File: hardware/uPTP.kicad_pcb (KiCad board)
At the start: 2 copper layers, 40 x 50 mm, 56 parts, among them J1 UART_HDR, J2 PPS_UFL, J3 PPS_SMA, J4 HC-RJ45-055-7, J5 AUX_PWR, J6 PROG, U1 CH32V307WCU6, U2 TMI7301, U3 LMR16030SDDAR, U4 XC6206P332MR-G, U5 SI3404-A-GMR, X1 X50328MSB2GI

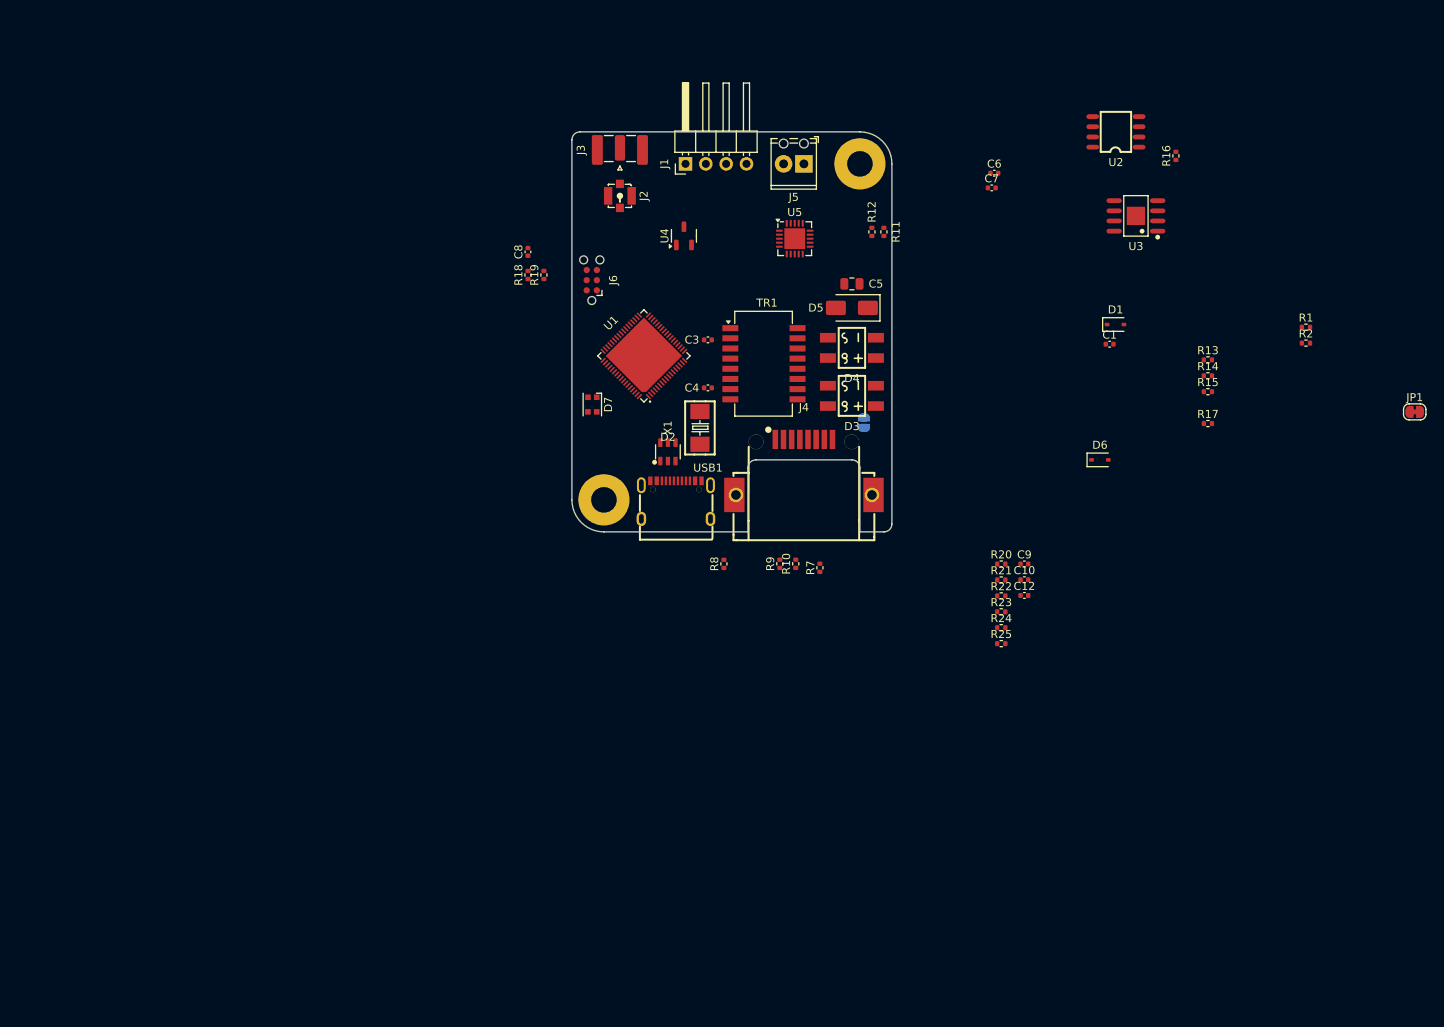
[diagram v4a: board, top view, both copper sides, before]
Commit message: Confirm all part footprints, start rought layout
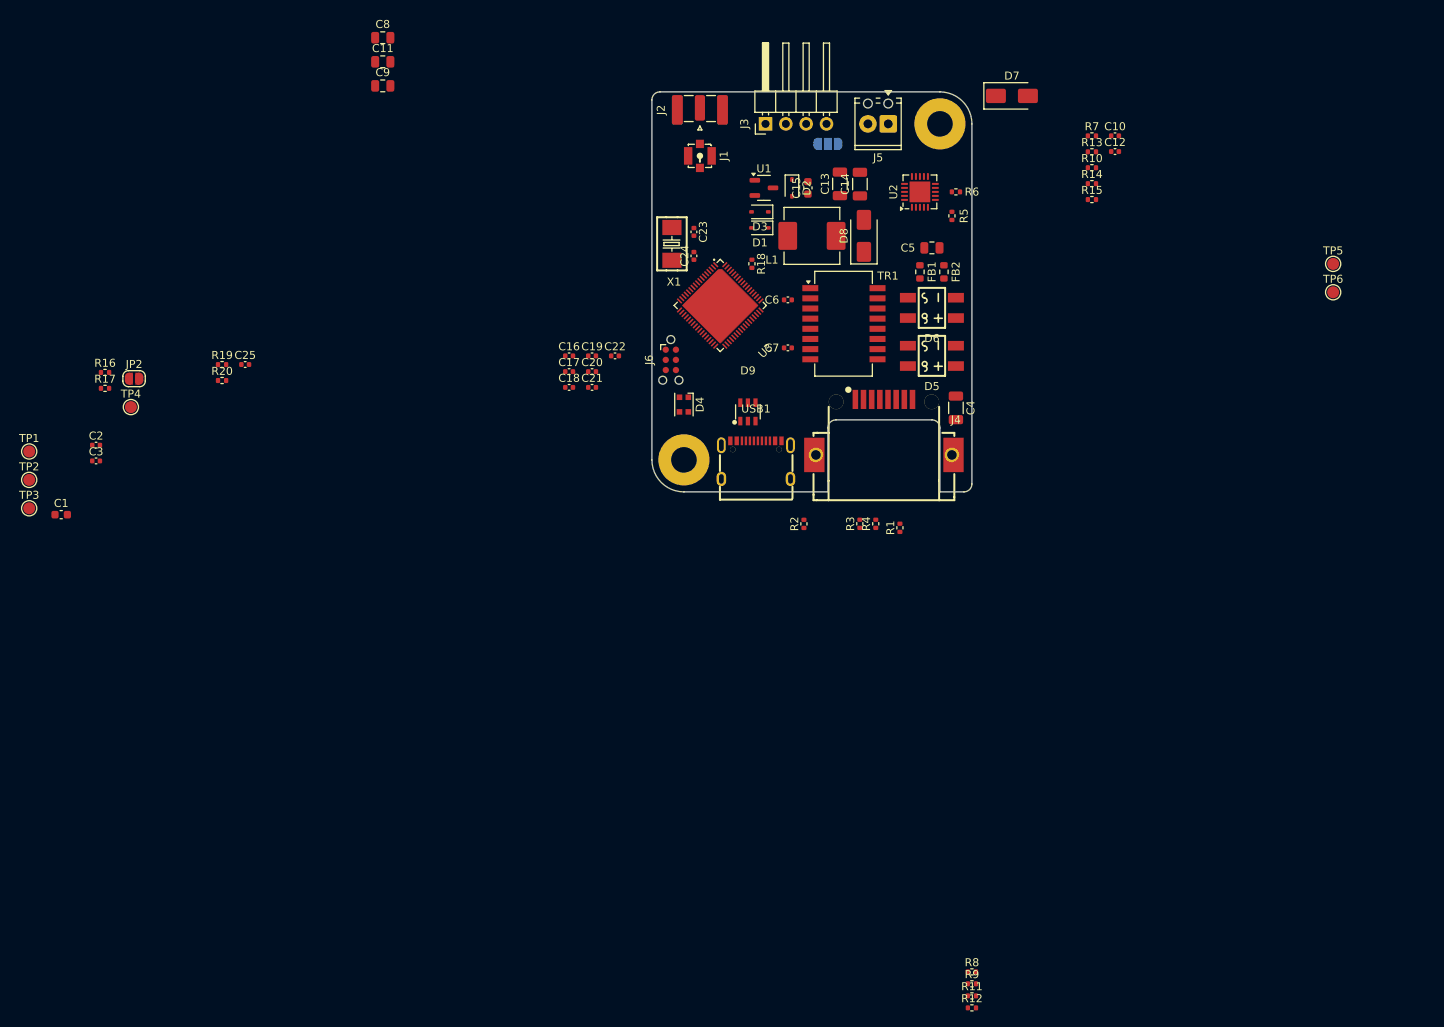
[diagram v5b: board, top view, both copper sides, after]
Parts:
- removed the C12 at (176.6, 137.9)
- removed the C6 at (172.8, 85.2)
- removed the C7 at (172.5, 87.0)
- removed the D5 at (155.0, 102.0)
- removed the D6 at (186.0, 121.0)
- removed the R1 at (211.8, 104.4)
- removed the R2 at (211.8, 106.4)
- removed R25: ?, Resistor_SMD:R_0402_1005Metric
- removed the U2 at (188.0, 80.0)
- removed U4: XC6206P332MR-G, Package_TO_SOT_SMD:SOT-23-3
- added C11: 10u, Capacitor_SMD:C_0805_2012Metric, F.Cu at (96.4, 71.2)
- added C13: 100u, Capacitor_SMD:C_1206_3216Metric, F.Cu at (153.5, 86.5)
- added C14: 100u, Capacitor_SMD:C_1206_3216Metric, F.Cu at (156.0, 86.5)
- added C15: 10u, Capacitor_SMD:C_0603_1608Metric, F.Cu at (149.5, 87.0)
- added C16: 100n, Capacitor_SMD:C_0402_1005Metric, F.Cu at (119.7, 108.0)
- added C17: 100n, Capacitor_SMD:C_0402_1005Metric, F.Cu at (119.7, 110.0)
- added C18: 100n, Capacitor_SMD:C_0402_1005Metric, F.Cu at (119.7, 111.9)
- added C19: 100n, Capacitor_SMD:C_0402_1005Metric, F.Cu at (122.5, 108.0)
- added C2: 100n, Capacitor_SMD:C_0402_1005Metric, F.Cu at (60.5, 119.2)
- added C20: 100n, Capacitor_SMD:C_0402_1005Metric, F.Cu at (122.5, 110.0)
- added C21: 100n, Capacitor_SMD:C_0402_1005Metric, F.Cu at (122.5, 111.9)
- added C22: 100n, Capacitor_SMD:C_0402_1005Metric, F.Cu at (125.4, 108.0)
- added C23: 20p, Capacitor_SMD:C_0402_1005Metric, F.Cu at (135.2, 92.5)
- added C24: 20p, Capacitor_SMD:C_0402_1005Metric, F.Cu at (135.2, 95.5)
- added C25: 100n, Capacitor_SMD:C_0402_1005Metric, F.Cu at (79.2, 109.1)
- added C3: 2.2u, Capacitor_SMD:C_0402_1005Metric, F.Cu at (60.5, 121.1)
- added C4: 1n, Capacitor_SMD:C_1206_3216Metric, F.Cu at (168.0, 114.5)
- added C9: 10u, Capacitor_SMD:C_0805_2012Metric, F.Cu at (96.4, 74.2)
- added D3: BAT60JFILM, Diode_SMD:D_SOD-323, F.Cu at (143.5, 90.0)
- added D7: SS210, Diode_SMD:D_SMA, F.Cu at (175.0, 75.5)
- added D8: SS210, Diode_SMD:D_SMA, F.Cu at (156.5, 93.0)
- added D9: USBLC6-2SC6, uPTP:SOT-23-6_L2.9-W1.6-P0.95-LS2.8-BL, F.Cu at (142.0, 115.0)
- added FB1: GZ1608D601TF, Resistor_SMD:R_0603_1608Metric, F.Cu at (163.5, 97.5)
- added FB2: GZ1608D601TF, Resistor_SMD:R_0603_1608Metric, F.Cu at (166.5, 97.5)
- added L1: 47u, Inductor_SMD:L_Changjiang_FXL0630, F.Cu at (150.0, 93.0)
- added R17: 10k, Resistor_SMD:R_0402_1005Metric, F.Cu at (61.6, 112.1)
- added R20: 5.1k, Resistor_SMD:R_0402_1005Metric, F.Cu at (76.3, 111.1)
- added TP1: 5V_EXT, TestPoint:TestPoint_Pad_D1.5mm, F.Cu at (52.2, 120.0)
- added TP2: LED_OUT, TestPoint:TestPoint_Pad_D1.5mm, F.Cu at (52.2, 123.5)
- added TP3: LED_GND, TestPoint:TestPoint_Pad_D1.5mm, F.Cu at (52.2, 127.0)
- added TP4: BOOT1, TestPoint:TestPoint_Pad_D1.5mm, F.Cu at (64.9, 114.4)
- added TP5: DEBUG_1, TestPoint:TestPoint_Pad_D1.5mm, F.Cu at (215.2, 96.5)
- added TP6: DEBUG_2, TestPoint:TestPoint_Pad_D1.5mm, F.Cu at (215.2, 100.0)
- C1: value 100n -> 10u; footprint Capacitor_SMD:C_0402_1005Metric -> Capacitor_SMD:C_0603_1608Metric
- C12: renamed from C10; value 100n -> 1n
- C5: value 100n 100V -> 100n
- C8: footprint Capacitor_SMD:C_0402_1005Metric -> Capacitor_SMD:C_0805_2012Metric
- D1: value D_Schottky -> BAT60JFILM
- D2: value USBLC6-2SC6 -> BAT60JFILM; footprint uPTP:SOT-23-6_L2.9-W1.6-P0.95-LS2.8-BL -> Diode_SMD:D_SOD-323
- JP1: value POE_ENABLE -> PWR_SELECT; footprint Jumper:SolderJumper-2_P1.3mm_Bridged_RoundedPad1.0x1.5mm -> Jumper:SolderJumper-3_P1.3mm_Open_RoundedPad1.0x1.5mm_NumberLabels; moved to B.Cu
- JP2: value SHIELD_BRIDGE -> BOOT_0; moved to F.Cu
- R14: renamed from R23; value ? -> 11k
- R15: renamed from R24; value ? -> 3.9k
- R16: value 100k -> 10k
- R18: value 10k -> ?
- R19: value 10k -> 5.1k
- U1: value CH32V307WCU6 -> XC6206P332MR-G; footprint uPTP:QFN-68_L8.0-W8.0-P0.40-BL-EP6.7 -> Package_TO_SOT_SMD:SOT-23-3
- U3: value LMR16030SDDAR -> CH32V307WCU6; footprint uPTP:SOIC-8_L4.9-W3.9-P1.27-LS6.0-BL-EP2.3 -> uPTP:QFN-68_L8.0-W8.0-P0.40-BL-EP6.7
- moved R16 136.6 mm to (61.6, 110.1), turned to 0 degrees
- moved C1 132.8 mm to (56.2, 127.8)
- moved JP2 91.4 mm to (65.3, 110.8), turned to 0 degrees
- moved R8 82.0 mm to (170.0, 185.0)
- moved R9 81.5 mm to (170.0, 186.5)
- moved R11 81.1 mm to (170.0, 188.0)
- moved JP1 80.6 mm to (152.0, 81.5)
- moved R12 78.8 mm to (170.0, 189.5)
- moved R14 54.7 mm to (185.0, 86.5)
- moved R7 54.7 mm to (185.0, 80.5)
- moved C10 54.7 mm to (187.9, 80.5)
- moved C12 54.7 mm to (187.9, 82.5)
- moved R10 54.7 mm to (185.0, 84.5)
- moved R13 54.7 mm to (185.0, 82.5)
- moved R15 54.7 mm to (185.0, 88.5)
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- renumbered C9 to C10, C3 to C6, C4 to C7, D7 to D4, D3 to D5, D4 to D6, J2 to J1, J3 to J2, J1 to J3, R7 to R1, R22 to R10, R15 to R11, R17 to R12, R21 to R13, R8 to R2, R9 to R3, R10 to R4, R11 to R5, R12 to R6, R20 to R7, R13 to R8, R14 to R9, U5 to U2
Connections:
- net Net-(D5-A2) renamed /Ethernet and POE/ETH_POE_FILT_N
- net Net-(U5-EROUT) renamed /Ethernet and POE/ETH_EROUT
- net Net-(U5-FBH) renamed /Ethernet and POE/ETH_5V_FB
- net Net-(U5-RFREQ) renamed /Ethernet and POE/RFREQ
- net Net-(U5-VDD) renamed /Ethernet and POE/ETH_VDD
- C1 pad 1: +5V_USB -> +5V
- C12 pad 2: Net-(C10-Pad2) -> /Ethernet and POE/ETH_EROUT_RC
- C5 pad 1: Net-(D5-A1) -> /Ethernet and POE/ETH_POE_FILT_P
- C8 pad 1: /~{RST} -> /Ethernet and POE/ETH_POE_FILT_P
- C8 pad 2: GND -> /Ethernet and POE/ETH_ISENSE
- D1 pad 1: unconnected-(D1-K-Pad1) -> +5V
- D1 pad 2: unconnected-(D1-A-Pad2) -> +5V_USB
- D2 pad 1: /USB_D_CONN_N -> +5V
- D2 pad 2: GND -> /Ethernet and POE/ETH_POE_FILT_P
- D4 pad 1: Net-(D7-DOUT) -> /LED_STAGE_2
- D4 pad 3: unconnected-(D7-DIN-Pad3) -> /LED_STAGE_1
- D4 pad 4: unconnected-(D7-VDD-Pad4) -> +5V
- J1 pad 1: /PPS_OUT -> /PPS
- J2 pad 1: /PPS_OUT -> /PPS
- J3 pad 2: /UART_TX -> /MCU/NMEA_UART_RX
- J3 pad 3: /UART_RX -> /MCU/NMEA_UART_TX
- J3 pad 4: +3V3 -> /UART_PWR
- J5 pad 1: GND -> /Ethernet and POE/ETH_EROUT_RC
- J5 pad 2: /Power/V_AUX -> Net-(D7-A)
- J6 pad 2: /SWCLK -> /MCU/SWDIO
- J6 pad 3: /~{RST} -> /MCU/~{RST}
- J6 pad 4: /SWDIO -> /MCU/SWCLK
- JP1 pad 1: /Ethernet and POE/V_POE -> +5V
- JP1 pad 2: /Power/V_POE -> /UART_PWR
- JP2 pad 1: SHIELD -> GND
- JP2 pad 2: GND -> /MCU/MCU_BOOT0
- R10 pad 1: Net-(U5-HSO) -> /Ethernet and POE/ETH_ISENSE
- R13 pad 1: Net-(C10-Pad2) -> /Ethernet and POE/ETH_EROUT_RC
- R14 pad 1: Net-(D5-A1) -> /Ethernet and POE/ETH_POE_FILT_P
- R15 pad 2: Net-(R24-Pad2) -> GND
- R16 pad 1: /Ethernet and POE/ETH_POE_P -> +3V3
- R16 pad 2: /Ethernet and POE/POE_READY -> /MCU/MCU_BOOT0
- R18 pad 1: +3V3 -> /PPS
- R18 pad 2: /~{RST} -> /MCU/PPS_MCU
- R19 pad 1: +3V3 -> /USB/USB_CC2
- R19 pad 2: Net-(U1-BOOT0) -> GND
- R5 pad 1: Net-(D5-A1) -> /Ethernet and POE/ETH_POE_FILT_P
- R7 pad 1: Net-(D5-A1) -> /Ethernet and POE/ETH_POE_FILT_P
- U1 pad 1: unconnected-(U1-VBAT-Pad1) -> GND
- U1 pad 2: unconnected-(U1-PC13-Pad2) -> +3V3
- U1 pad 3: unconnected-(U1-PC14-Pad3) -> +5V
- U2 pad 1: Net-(U5-HSO) -> /Ethernet and POE/ETH_ISENSE
- U2 pad 13: Net-(D5-A1) -> /Ethernet and POE/ETH_POE_FILT_P
- U2 pad 18: Net-(D8-A) -> /Ethernet and POE/ETH_BUCK_SW
- U2 pad 8: Net-(U5-HSO) -> /Ethernet and POE/ETH_ISENSE
- U3 pad 1: unconnected-(U3-BOOT-Pad1) -> +3V3
- U3 pad 5: unconnected-(U3-FB-Pad5) -> /MCU/XTAL_IN
- U3 pad 6: unconnected-(U3-SS-Pad6) -> /MCU/XTAL_OUT
- U3 pad 7: unconnected-(U3-GND-Pad7) -> /MCU/~{RST}
- USB1 pad 10: Net-(USB1-CC2) -> /USB/USB_CC2
- USB1 pad 4: Net-(USB1-CC1) -> /USB/USB_CC1
- USB1 pad 5: /USB_D_CONN_N -> /USB/USB_D_CONN_N
- USB1 pad 6: /USB_D_CONN_P -> /USB/USB_D_CONN_P
- USB1 pad 7: /USB_D_CONN_N -> /USB/USB_D_CONN_N
- USB1 pad 8: /USB_D_CONN_P -> /USB/USB_D_CONN_P
- X1 pad 1: /XTAL_IN -> /MCU/XTAL_IN
- X1 pad 2: /XTAL_OUT -> /MCU/XTAL_OUT

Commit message: Tidy up layout
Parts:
- removed the TP2 at (52.2, 123.5)
- removed the TP3 at (52.2, 127.0)
- added J3: LED, Connector_PinHeader_1.27mm:PinHeader_1x03_P1.27mm_Vertical, F.Cu at (138.8, 115.0)
- JP2, TP1: moved to B.Cu
- TP2: renamed from TP4; moved to B.Cu
- TP3: renamed from TP5; moved to B.Cu
- TP4: renamed from TP6; moved to B.Cu
- moved TP1 100.0 mm to (146.0, 85.5)
- moved C1 99.1 mm to (144.5, 83.0), turned to 180 degrees
- moved C2 91.3 mm to (145.0, 84.5), turned to 180 degrees
- moved C3 87.4 mm to (141.0, 87.0), turned to 90 degrees
- moved TP3 82.8 mm to (132.5, 102.0)
- moved TP4 82.8 mm to (132.5, 105.0)
- moved R16 80.5 mm to (141.0, 96.5), turned to -90 degrees
- moved JP2 77.1 mm to (141.0, 96.5), turned to -90 degrees
- moved R17 72.9 mm to (133.5, 99.8)
- moved R19 69.7 mm to (145.5, 117.0)
- moved C9 68.7 mm to (162.0, 94.5), turned to 90 degrees
- moved C8 68.2 mm to (160.5, 91.5)
- moved TP2 67.9 mm to (132.5, 108.0)
- moved C11 67.3 mm to (159.5, 94.5), turned to -90 degrees
- moved R20 65.0 mm to (141.0, 117.0), turned to 180 degrees
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- renumbered J3 to J4, J4 to J5, J5 to J6, J6 to J7
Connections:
- net Net-(D7-A) renamed /Ethernet and POE/ETH_AUX
- TP3 pad 1: unconnected-(TP5-Pad1) -> /MCU/DEBUG_1
- TP4 pad 1: unconnected-(TP6-Pad1) -> /MCU/DEBUG_2
- U3 pad 22: unconnected-(U3-PA6-Pad22) -> /MCU/DEBUG_1
- U3 pad 23: unconnected-(U3-PA7-Pad23) -> /MCU/DEBUG_2
- U3 pad 36: unconnected-(U3-PB13-Pad36) -> /LED_STAGE_1
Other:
- board text removed: "TODO line up to 2.54mm grid"

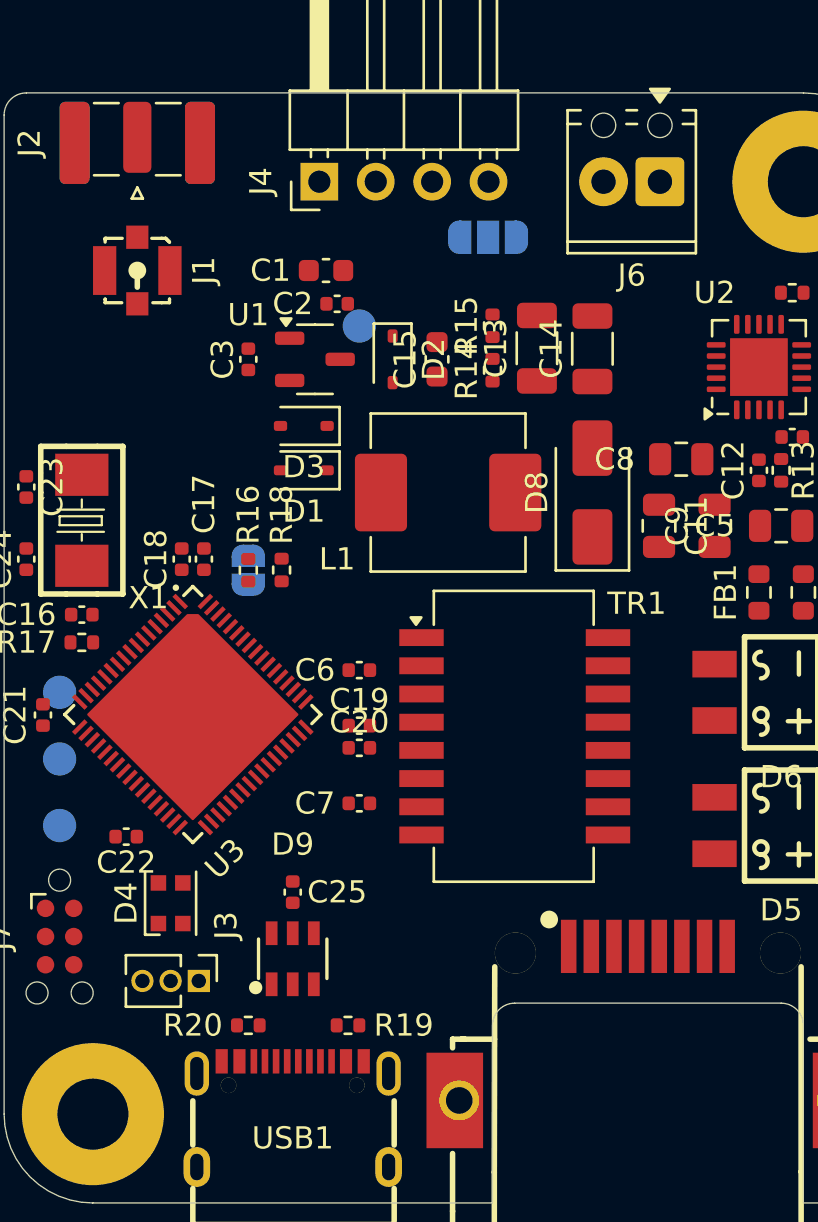
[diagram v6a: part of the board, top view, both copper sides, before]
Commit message: Set reqs for trace widths
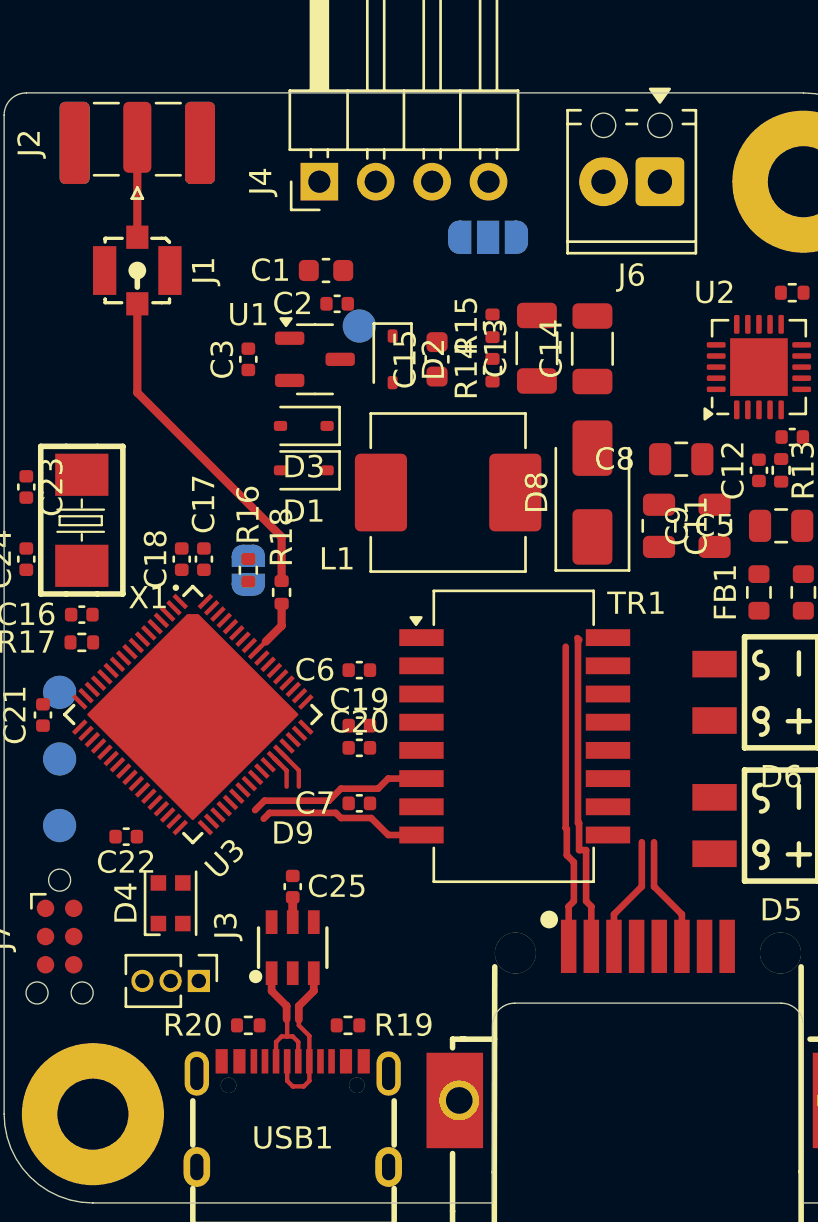
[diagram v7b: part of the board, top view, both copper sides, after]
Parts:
- moved R18 1.01 mm to (142.5, 97.5)
- moved D9 0.50 mm to (143.0, 113.5)
- moved C25 0.25 mm to (143.0, 110.8)
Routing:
- net /PPS: track 0.00 -> 19.7 mm
- net /Ethernet and POE/ETH_D_ISO_TX_N: track 0.00 -> 14.4 mm
- net /Ethernet and POE/ETH_D_ISO_TX_P: track 0.00 -> 13.7 mm
- net /Ethernet and POE/ETH_D_RX_P: track 0.00 -> 8.08 mm
- net /Ethernet and POE/ETH_D_RX_N: track 0.00 -> 7.63 mm
- net /USB/USB_D_CONN_P: track 0.00 -> 7.41 mm
- net /USB/USB_D_CONN_N: track 0.00 -> 6.09 mm
- net /Ethernet and POE/ETH_D_ISO_RX_P: track 0.00 -> 5.21 mm
- net /Ethernet and POE/ETH_D_ISO_RX_N: track 0.00 -> 5.21 mm
- net /MCU/PPS_MCU: track 0.00 -> 2.65 mm
- net /MCU/USB_D_N: track 0.00 -> 1.89 mm
- net /MCU/USB_D_P: track 0.00 -> 1.50 mm
- net +5V_USB: track 0.00 -> 1.12 mm
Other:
- copper layers 2 -> 4
